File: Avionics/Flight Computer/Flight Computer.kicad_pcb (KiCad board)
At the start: 4 copper layers, 50 x 40 mm, 178 parts, among them J1 ERF8-040-05.0-S-DV-K, J2 ERF8-040-05.0-S-DV-K, J3 473460001, J4 734120110, J5 0734120110, J6 734120110, U1 CC1310F128RGZR, U12 ATSAME70Q21A-AN, U2 CC1190RGVR, U3 CC2650F128RGZR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

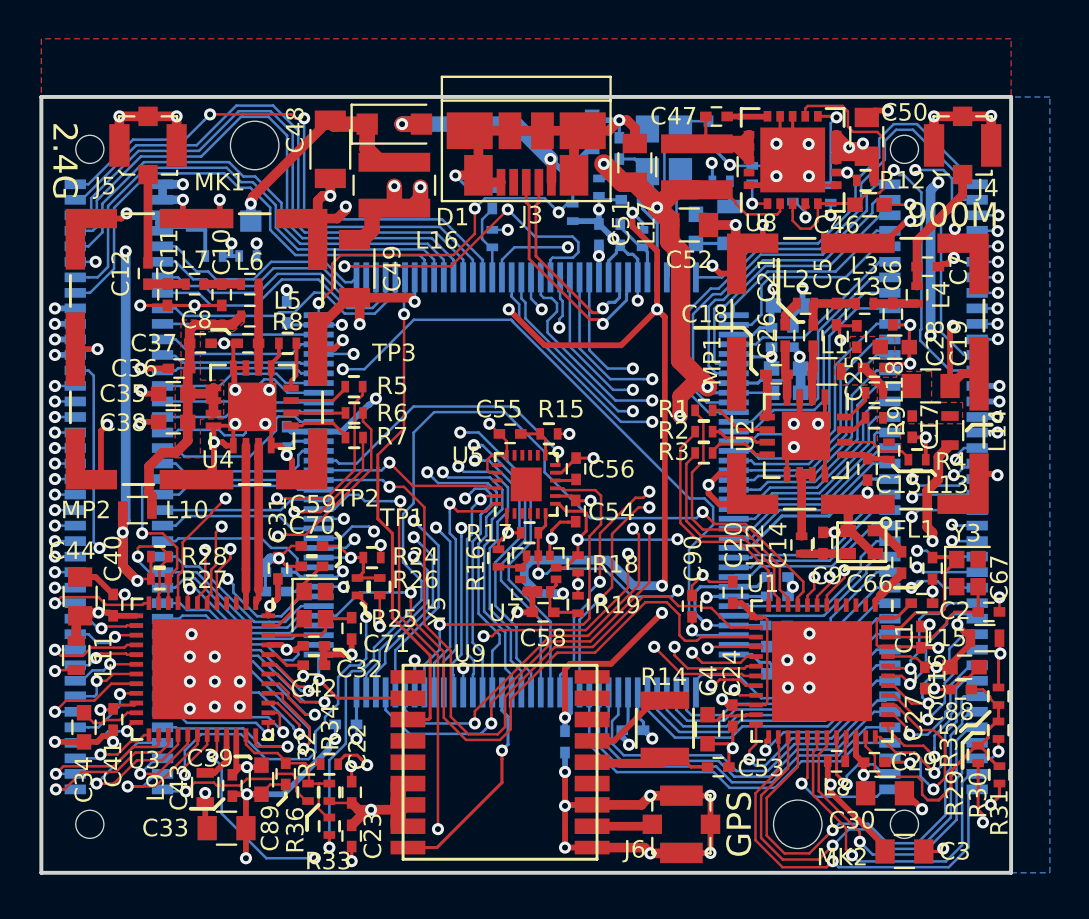
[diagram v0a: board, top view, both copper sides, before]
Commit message: Added LEDs
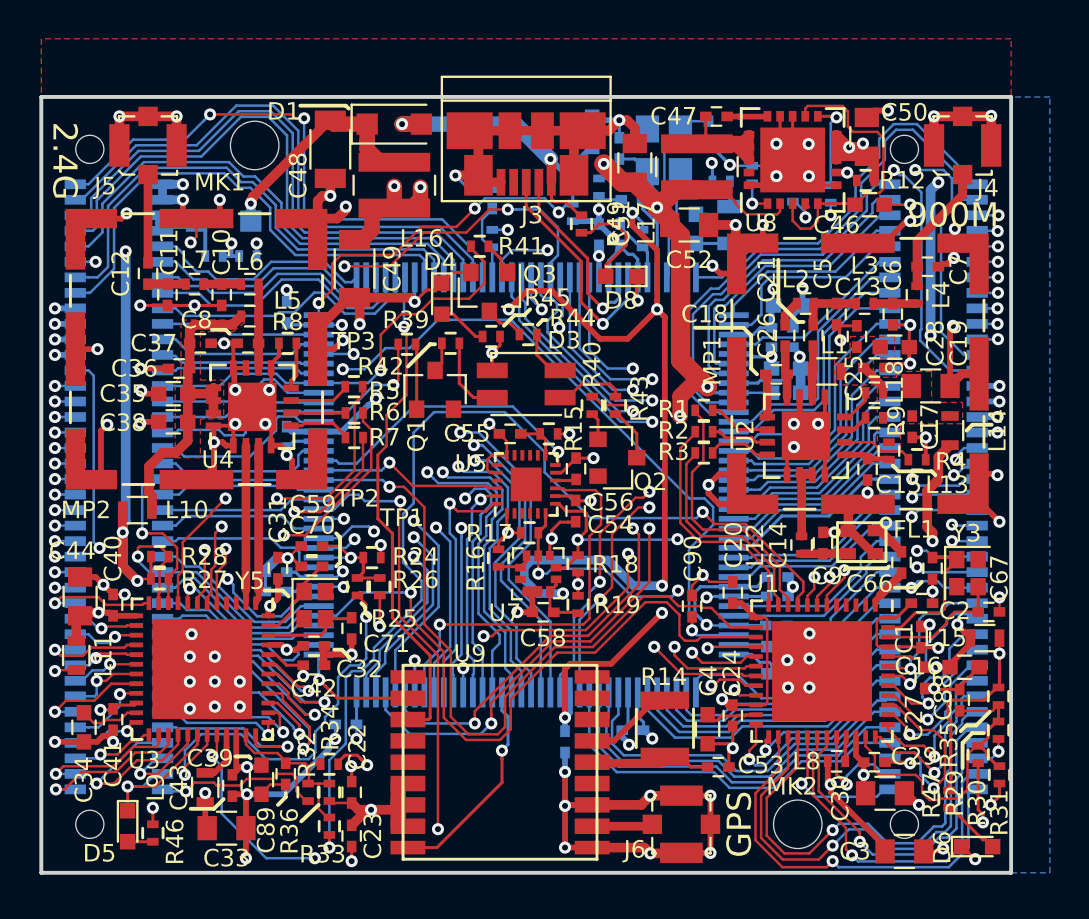
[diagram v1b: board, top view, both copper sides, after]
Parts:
- added D3: CLV1L-FKB, LEDs:LED_Cree-PLCC4_3.2x2.8mm, F.Cu at (75.0, 99.8)
- added D4: LED-0603-GREEN, LEDs:LED_0603, F.Cu at (70.7, 95.4)
- added D5: LED-0603-GREEN, LEDs:LED_0603, F.Cu at (54.5, 122.6)
- added D6: LED-0603-RED, LEDs:LED_0603, F.Cu at (98.2, 123.7)
- added D8: LED-0603-GREEN, LEDs:LED_0603, F.Cu at (79.9, 94.2)
- added Q1: MMBT3904L, TO_SOT_Packages_SMD:SOT-23, F.Cu at (70.3, 100.1)
- added Q2: MMBT3904L, TO_SOT_Packages_SMD:SOT-23, F.Cu at (79.7, 103.6)
- added Q3: MMBT3904L, TO_SOT_Packages_SMD:SOT-23, F.Cu at (73.1, 95.0)
- added R39: 10k, Resistors_SMD:R_0402, F.Cu at (68.8, 97.8)
- added R40: 10k, Resistors_SMD:R_0402, F.Cu at (78.4, 100.9)
- added R41: 10k, Resistors_SMD:R_0402, F.Cu at (72.6, 92.7)
- added R42: 1k, Resistors_SMD:R_0402, F.Cu at (71.1, 97.7)
- added R43: 1k, Resistors_SMD:R_0402, F.Cu at (79.6, 100.9)
- added R44: 1k, Resistors_SMD:R_0402, F.Cu at (75.1, 97.2)
- added R45: 10k, Resistors_SMD:R_0402, F.Cu at (73.2, 97.3)
- added R46: 1k, Resistors_SMD:R_0402, F.Cu at (55.8, 123.0)
- added R47: 1k, Resistors_SMD:R_0402, F.Cu at (96.8, 121.2)
- added R49: 10k, Resistors_SMD:R_0402, F.Cu at (77.8, 91.5)
- R4: value 3.35 -> 3.3k
- moved C88 0.55 mm to (97.3, 116.1), turned to 90 degrees
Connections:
- net /Connectors/2.4-DIO-20 renamed /2.4-DIO-20
- net /Connectors/900-DIO-20 renamed /900-DIO-20
- net /Connectors/PD10 renamed /PD10
- net /Connectors/PD11 renamed /PD11
- net /Connectors/PD4 renamed /PD4
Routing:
- net /PD10: track 8.51 -> 22.5 mm, vias 0 -> 1
- net +3V3: track 128.3 -> 138.5 mm, vias 29 -> 31
- net /900-DIO-20: track 17.4 -> 24.8 mm, vias 1 -> 2
- net GND: track 297.6 -> 304.8 mm, vias 112 -> 115
- net /PD11: track 8.91 -> 15.5 mm, vias 0 -> 1
- net Net-(D8-Pad2): track 0.00 -> 5.30 mm
- net Net-(D3-Pad2): track 0.00 -> 4.07 mm
- net Net-(D3-Pad3): track 0.00 -> 3.62 mm
- net Net-(Q1-Pad1): track 0.00 -> 3.37 mm
- net Net-(D6-Pad2): track 0.00 -> 3.23 mm
- net Net-(Q2-Pad3): track 0.00 -> 2.76 mm
- net VUSB: track 13.5 -> 16.3 mm
- net Net-(D3-Pad4): track 0.00 -> 2.58 mm
- net Net-(D4-Pad2): track 0.00 -> 2.58 mm
- net /PD4: track 32.1 -> 34.5 mm
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
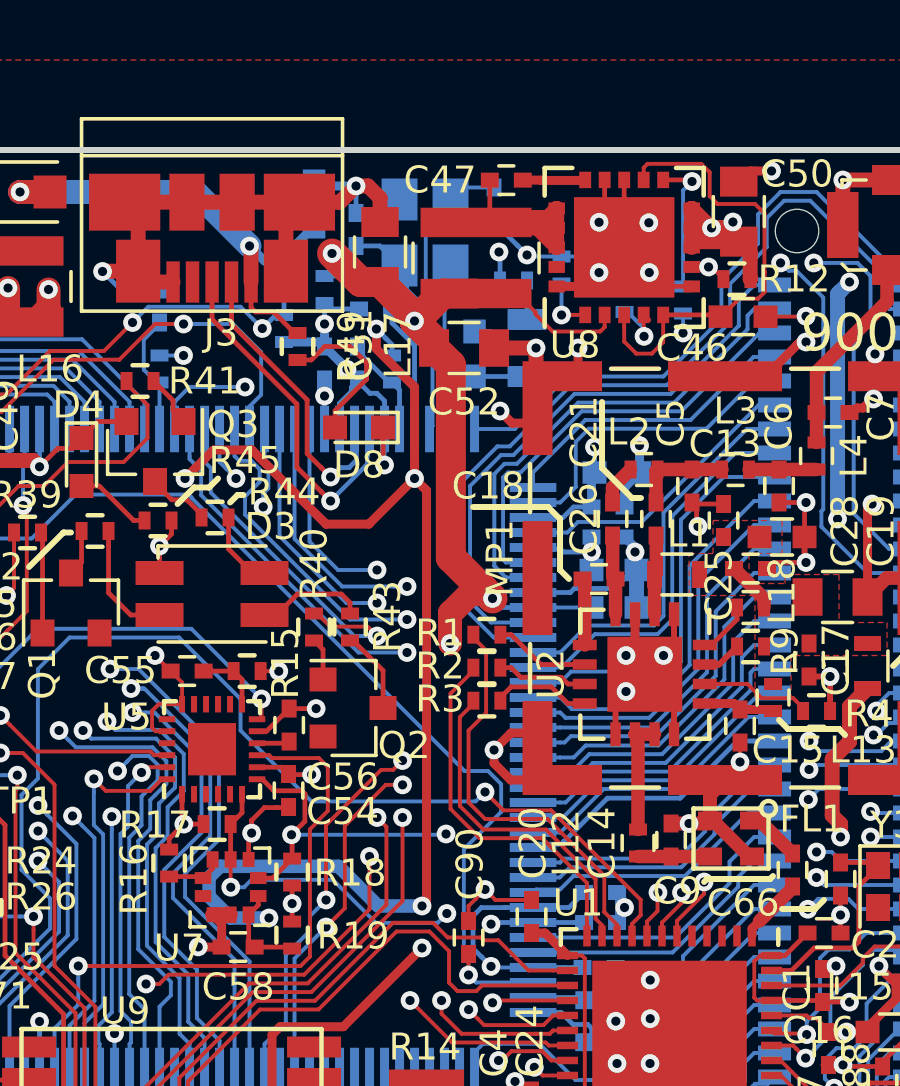
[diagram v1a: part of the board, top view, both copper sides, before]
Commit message: Cleaned up silk and DRC for new components.
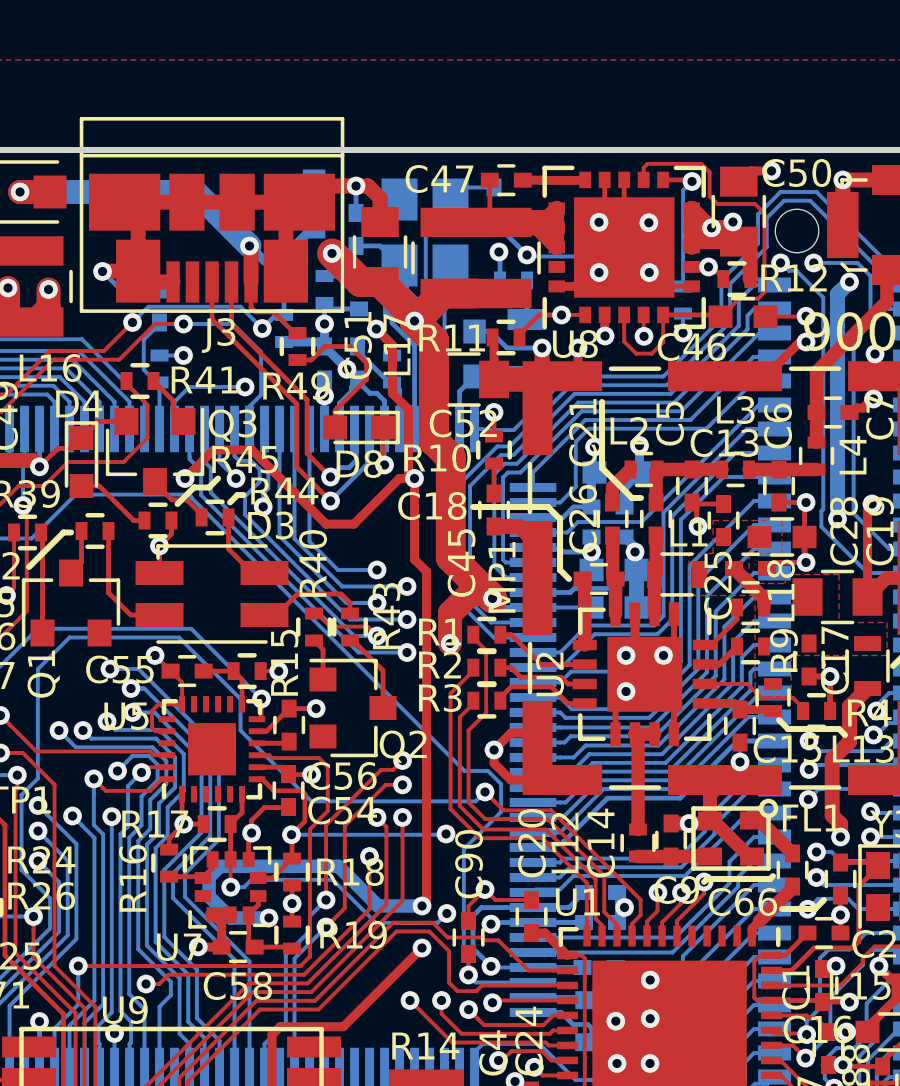
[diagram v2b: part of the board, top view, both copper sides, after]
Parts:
- C45, R10, R11: moved to F.Cu
- moved C45 10.0 mm to (84.4, 97.0), turned to 270 degrees
- moved R10 6.67 mm to (84.4, 95.0), turned to 270 degrees
- moved R11 2.91 mm to (84.8, 91.2), turned to 180 degrees
- moved C52 1.05 mm to (83.4, 92.7)
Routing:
- net Net-(R10-Pad1): track 2.10 -> 7.84 mm, vias 1 -> 2
- net GND: track 304.8 -> 309.3 mm, vias 115 -> 114
- net +3V3: track 138.5 -> 135.3 mm, vias 31 -> 32
- net Net-(R11-Pad1): track 1.84 -> 2.56 mm

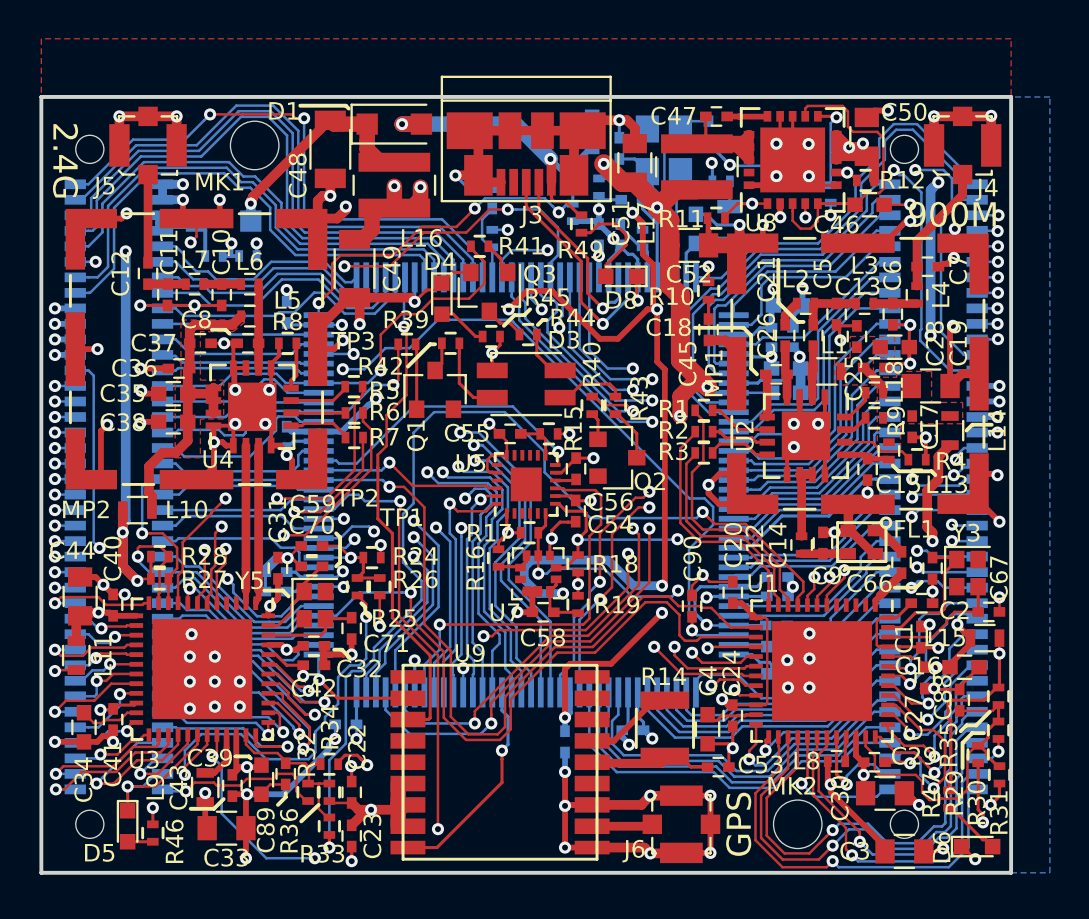
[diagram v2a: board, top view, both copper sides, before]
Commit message: Changed LED configuration, added smart driver chip to let all the CPUs access it..
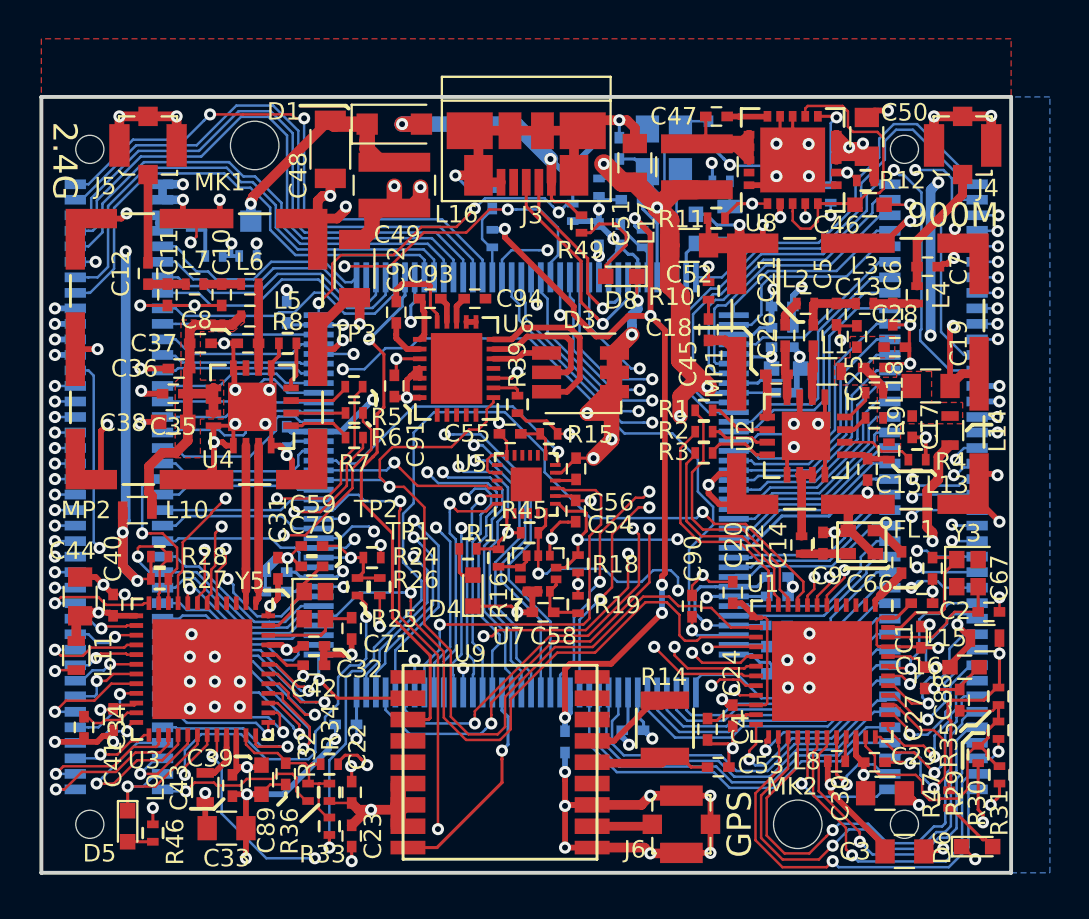
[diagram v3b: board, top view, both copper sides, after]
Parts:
- removed Q1, Q2, Q3: MMBT3904L, TO_SOT_Packages_SMD:SOT-23
- removed R40, R41: 10k, Resistors_SMD:R_0402
- removed R42, R43, R44: 1k, Resistors_SMD:R_0402
- added C91: 1u, Capacitors_SMD:C_0402, F.Cu at (68.2, 99.9)
- added C92: 0.47u, Capacitors_SMD:C_0402, F.Cu at (68.3, 96.1)
- added C93: 0.47u, Capacitors_SMD:C_0402, F.Cu at (70.0, 95.4)
- added C94: 1u, Capacitors_SMD:C_0402, F.Cu at (72.3, 95.4)
- added U6: LP5521YQ, Housings_DFN_QFN:QFN-24-1EP_4x5mm_Pitch0.5mm, F.Cu at (71.4, 99.0)
- C28, C34, C35, C4, C61, C68, C87: footprint Capacitors_SMD:C_0603 -> Capacitors_SMD:C_0402
- D3: value CLV1L-FKB -> CLX6D-FKB; footprint LEDs:LED_Cree-PLCC4_3.2x2.8mm -> LEDs:LED_PLCC6_3.4x3.4mm
- moved D4 15.1 mm to (72.2, 110.5), turned to 90 degrees
- moved R45 11.0 mm to (72.0, 108.3)
- moved R39 6.49 mm to (74.5, 100.8), turned to 90 degrees
- moved D3 2.86 mm to (77.8, 99.2), turned to 180 degrees
- moved C68 0.30 mm to (88.2, 95.8), turned to 0 degrees
- turned C61 to 90 degrees
- turned C87 to 0 degrees
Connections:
- net /2.4-DIO-20 renamed /Connectors/2.4-DIO-20
- net /900-DIO-20 renamed /Connectors/900-DIO-20
- net /PD10 renamed /Connectors/PD10
- net /PD4 renamed /Connectors/PD4
- C61 pad 1: GND -> VUSB
- C61 pad 2: VUSB -> GND
- C68 pad 1: GND -> Net-(C57-Pad1)
- C68 pad 2: Net-(C57-Pad1) -> GND
- C87 pad 1: GND -> +3V3
- C87 pad 2: +3V3 -> GND
- D3 pad 1: +3V3 -> GND
- D3 pad 2: Net-(D3-Pad2) -> GND
- D3 pad 3: Net-(D3-Pad3) -> GND
- J1 pad 33: /PD11 -> /Connectors/PD11
- R39 pad 1: Net-(Q1-Pad1) -> +3V3
- R39 pad 2: /PD11 -> Net-(R39-Pad2)
- U12 pad 98: /PD11 -> /Connectors/PD11
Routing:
- net /CPU-SCK: track 50.5 -> 66.5 mm, vias 2 -> 3
- net /PD11: track 15.5 -> 0.00 mm, vias 1 -> 0
- net /Connectors/PD10: track 22.5 -> 8.51 mm, vias 1 -> 0
- net GND: track 309.3 -> 322.9 mm, vias 114 -> 118
- net /CPU-SDA: track 54.9 -> 64.2 mm
- net Net-(D3-Pad6): track 0.00 -> 9.03 mm
- net /Connectors/PD11: track 0.00 -> 8.91 mm
- net Net-(D3-Pad5): track 0.00 -> 7.10 mm
- net Net-(C57-Pad1): track 107.8 -> 101.4 mm, vias 12 -> 10
- net Net-(C92-Pad2): track 0.00 -> 4.51 mm
- net Net-(D3-Pad2): track 4.07 -> 0.00 mm
- net +3V3: track 135.3 -> 138.9 mm
- net Net-(D3-Pad3): track 3.62 -> 0.00 mm
- net Net-(Q1-Pad1): track 3.37 -> 0.00 mm
- net Net-(Q2-Pad3): track 2.76 -> 0.00 mm
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
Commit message: DFM/BOM Optimizations
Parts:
- J5: value 0734120110 -> 734120110
- R10: value 20k -> 18k
- R11: value 12k -> 15k
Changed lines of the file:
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@@
   )
   (setup
-    (last_trace_width 0.8)
+    (last_trace_width 0.16)
     (user_trace_width 0.13)
     (user_trace_width 0.16)
@@
     )
   )
-  (module Connectors_Molex:Molex_Microcoaxial_RF locked (layer F.Cu)
+  (module Connectors_Molex:Molex_Microcoaxial_RF (layer F.Cu)
     (at 97.500526 87.499723)
     (descr "Molex Microcoaxial RF, mates Hirose U.FL, http://www.molex.com/pdm_docs/sd/734120110_sd.pdf")
@@
       (effects (font (size 0.9 0.9) (thickness 0.1)))
     )
-    (fp_text value 0734120110 (at 0 -3.302) (layer F.Fab)
+    (fp_text value 734120110 (at 0 -3.302) (layer F.Fab)
       (effects (font (size 0.9 0.9) (thickness 0.1)))
     )
@@
       (effects (font (size 0.9 0.9) (thickness 0.1)))
     )
-    (fp_text value 12k (at 0 1.8 180) (layer F.Fab)
+    (fp_text value 15k (at 0 1.8 180) (layer F.Fab)
       (effects (font (size 0.9 0.9) (thickness 0.1)))
     )
@@
       (effects (font (size 0.9 0.9) (thickness 0.1)))
     )
-    (fp_text value 20k (at 0 1.8 270) (layer F.Fab)
+    (fp_text value 18k (at 0 1.8 270) (layer F.Fab)
       (effects (font (size 0.9 0.9) (thickness 0.1)))
     )
